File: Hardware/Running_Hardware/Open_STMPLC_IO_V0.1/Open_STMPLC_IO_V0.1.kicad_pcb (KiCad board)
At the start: 2 copper layers, 169 x 90 mm, 546 parts, among them J1 Screw_Terminal_01x10, J2 Screw_Terminal_01x06, J3 Screw_Terminal_01x04, J33 Screw_Terminal_01x02, J34 Screw_Terminal_01x02, J35 Screw_Terminal_01x03, J36 Screw_Terminal_01x03, J37 Screw_Terminal_01x03, J38 Screw_Terminal_01x03, J39 10144517-041802LF, J4 Screw_Terminal_01x02, J40 Screw_Terminal_01x04, J41 10144517-041802LF, J42 10144517-041802LF, J43 Screw_Terminal_01x02, J5 Screw_Terminal_01x04, J6 Screw_Terminal_01x04, J7 Screw_Terminal_01x04, J8 Screw_Terminal_01x04, Q1 2N7002K, Q2 2N7002K, Q3 2N7002K, Q4 2N7002K, Q5 AOD407, Q6 AOD407, Q7 MMBT5401, U1 TPS1H200A, U10 MAX31865xTP, U11 MAX31856, U12 6N137, U13 TPS1H200A, U14 TPS26600PWP, U15 NVTFS5124PLTAG, U16 TPS26600PWP, U17 NVTFS5124PLTAG, U18 TPS26600PWP, U19 NVTFS5124PLTAG, U2 TPS1H200A, U20 6N137, U21 6N137, U22 6N137, U23 6N137, U24 6N137, U25 6N137, U26 6N137, U27 6N137, U28 6N137, U29 6N137, U3 TPS1H200A, U30 6N137, U37 XTR305, U38 XTR305, U39 AD4111, U4 TPS1H200A, U40 REF3025, U41 MAX31865xTP, U5 TPS1H200A, U6 TPS1H200A, U7 TPS26600PWP, U8 NVTFS5124PLTAG, U9 TPS1H200A, Y2 16MHz

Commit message: IO board layout 1
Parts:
- added D92: SMF5V0A, Diode_SMD:D_SMF, F.Cu at (166.5, 138.5)
- added D93: SMF5V0A, Diode_SMD:D_SMF, F.Cu at (170.0, 138.5)
- added D94: SMF5V0A, Diode_SMD:D_SMF, F.Cu at (174.0, 138.5)
- added D95: SMF5V0A, Diode_SMD:D_SMF, F.Cu at (178.0, 138.5)
- added D96: SMF5V0A, Diode_SMD:D_SMF, F.Cu at (183.5, 138.5)
- added D97: SMF5V0A, Diode_SMD:D_SMF, F.Cu at (187.0, 138.5)
- added D98: SMF5V0A, Diode_SMD:D_SMF, F.Cu at (191.0, 138.5)
- added D99: SMF5V0A, Diode_SMD:D_SMF, F.Cu at (195.0, 138.5)
- C46, C47, C48, C50, C51, C69, C70, C71, C72, C73, C74, C75, C76, C77, C78, C79, C80, C90, D118, D119, D120, D121, D122, D123, D124, D125, D159, D160, D90, D91, F1, F2, F3, F4, F5, FB4, Q5, Q6, Q7, R158, R159, R160, R161, R162, R192, R193, R194, R195, R196, R197, R198, R199, R200, R201, R202, R203, R245: moved to B.Cu
- C89: value 470uF/50V -> 220uF/50V; footprint Capacitor_THT:CP_Radial_D10.0mm_P5.00mm -> Capacitor_SMD:CP_Elec_10x10.5; moved to B.Cu
- moved FB1 228.7 mm to (205.9, 127.4), turned to -90 degrees
- moved C6 228.3 mm to (204.9, 131.9), turned to 90 degrees
- moved C4 226.7 mm to (205.9, 119.4), turned to -90 degrees
- moved J4 225.7 mm to (200.0, 145.4), turned to 0 degrees
- moved R21 225.6 mm to (202.9, 134.9), turned to -90 degrees
- moved D10 225.6 mm to (201.9, 138.9), turned to 180 degrees
- moved C5 223.7 mm to (203.4, 127.4), turned to -90 degrees
- moved C7 222.0 mm to (201.9, 130.9), turned to 180 degrees
- moved R23 221.7 mm to (200.9, 134.9), turned to -90 degrees
- moved U11 219.2 mm to (201.9, 121.4), turned to 90 degrees
- moved R24 216.8 mm to (199.9, 127.4), turned to 90 degrees
- moved C11 216.5 mm to (198.9, 131.9), turned to -90 degrees
- moved D159 187.9 mm to (204.0, 87.5)
- moved D160 183.1 mm to (207.5, 70.5)
- moved R161 174.1 mm to (203.0, 85.0), turned to 180 degrees
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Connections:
- F1 pad 1: Net-(J35-Pin_3) -> Net-(J35-Pin_1)
- F2 pad 1: Net-(J36-Pin_3) -> Net-(J36-Pin_1)
- F3 pad 1: Net-(J37-Pin_3) -> Net-(J37-Pin_1)
- F4 pad 1: Net-(J38-Pin_3) -> Net-(J38-Pin_1)
- J35 pad 1: GND -> Net-(J35-Pin_1)
- J35 pad 3: Net-(J35-Pin_3) -> GND
- J36 pad 1: GND -> Net-(J36-Pin_1)
- J36 pad 3: Net-(J36-Pin_3) -> GND
- J37 pad 1: GND -> Net-(J37-Pin_1)
- J37 pad 3: Net-(J37-Pin_3) -> GND
- J38 pad 1: GND -> Net-(J38-Pin_1)
- J38 pad 3: Net-(J38-Pin_3) -> GND
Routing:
- net /DIG_IN_GRP2/COMD: track 0.00 -> 74.1 mm, vias 0 -> 1
- net /DIG_IN_GRP1/COMA: track 0.00 -> 64.3 mm, vias 0 -> 1
- net /DIG_IN_GRP2/DIG_IN_TERMINAL_12: track 0.00 -> 43.2 mm
- net /ANALOG_IN/VIN4: track 4.96 -> 46.6 mm, vias 0 -> 1
- net /DIG_IN_GRP1/DIG_IN_TERMINAL_1: track 0.00 -> 39.8 mm
- net /DIG_IN_GRP1/COMB: track 0.00 -> 39.5 mm, vias 0 -> 1
- net /DIG_IN_GRP2/COMC: track 0.00 -> 39.0 mm
- net /ANALOG_IN/VIN0: track 6.98 -> 44.4 mm, vias 0 -> 1
- net +3V3: track 145.9 -> 180.8 mm
- net /DIG_IN_GRP2/DIG_IN_TERMINAL_11: track 0.00 -> 34.4 mm
- net /DIG_IN_GRP1/DIG_IN_TERMINAL_2: track 0.00 -> 31.2 mm
- net /ANALOG_IN/IIN0+: track 0.00 -> 31.1 mm, vias 0 -> 1
- net /B2B_Connector/DIG_OUT_TERMINAL_8: track 7.88 -> 38.4 mm
- net /B2B_Connector/DIG_HS_OUT_TERMINAL_1: track 9.66 -> 39.6 mm
- net /B2B_Connector/DIG_OUT_TERMINAL_1: track 7.88 -> 37.4 mm
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
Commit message: LED arrengements
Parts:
- J39, J41, J42: moved to B.Cu
- moved D113 14.6 mm to (101.5, 125.5), turned to 90 degrees
- moved D108 14.3 mm to (80.0, 125.5), turned to 90 degrees
- moved U37 6.04 mm to (70.2, 112.1)
- moved C52 6.04 mm to (76.5, 109.5)
- moved C53 6.04 mm to (74.5, 113.0)
- moved C54 6.04 mm to (78.5, 113.0)
- moved C55 6.04 mm to (69.0, 117.0)
- moved C56 6.04 mm to (76.5, 116.0)
- moved C57 6.04 mm to (74.5, 109.5)
- moved D109 6.04 mm to (66.6, 125.5)
- moved D110 6.04 mm to (71.1, 125.5)
- moved D111 6.04 mm to (75.6, 125.5)
- moved R164 6.04 mm to (72.5, 117.0)
- moved R165 6.04 mm to (71.5, 106.5)
- moved R166 6.04 mm to (69.5, 106.5)
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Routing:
- net Net-(D112-A2): track 28.8 -> 34.8 mm
- net Net-(D114-A2): track 28.8 -> 34.8 mm
- net Net-(D114-A1): track 12.7 -> 18.7 mm
- net Net-(D110-K): track 12.7 -> 18.7 mm
- net /B2B_Connector/DIG_OUT_TERMINAL_8: track 38.4 -> 44.4 mm
- net /B2B_Connector/DIG_OUT_TERMINAL_5: track 17.2 -> 23.2 mm
- net /B2B_Connector/DIG_OUT_TERMINAL_4: track 16.7 -> 22.7 mm
- net /B2B_Connector/DIG_OUT_TERMINAL_1: track 37.4 -> 43.4 mm
- net /B2B_Connector/DIG_OUT_TERMINAL_2: track 30.0 -> 35.4 mm
- net +3V3: track 180.8 -> 175.6 mm
- net Net-(U38-SET): track 25.8 -> 29.2 mm, vias 2 -> 3
- net /ANALOG_OUT/AOUT2_V-: track 31.3 -> 34.2 mm
- net /B2B_Connector/DIG_OUT_TERMINAL_3: track 22.8 -> 25.7 mm
- net /ANALOG_IN/VIN4: track 46.6 -> 49.2 mm
- net /B2B_Connector/DIG_OUT_TERMINAL_6: track 23.6 -> 26.2 mm
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
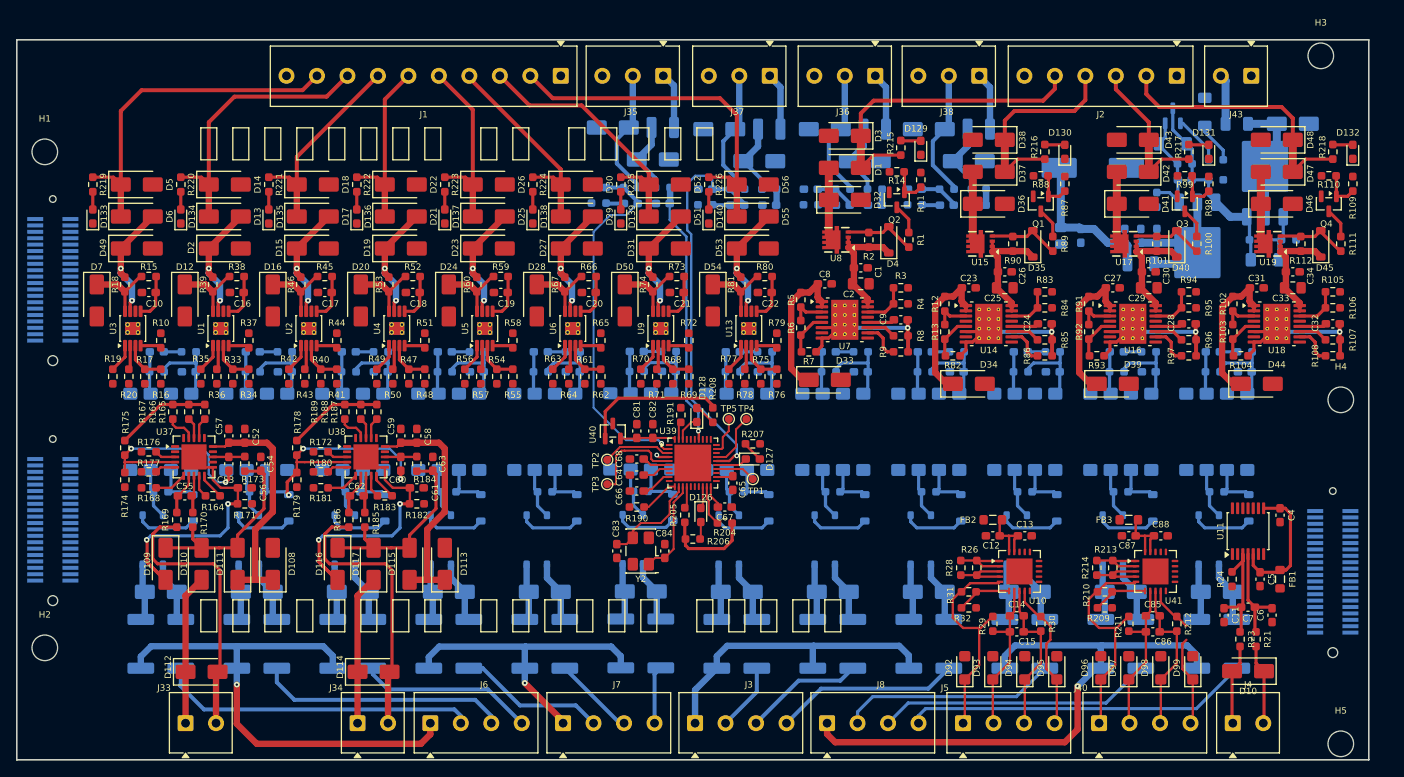
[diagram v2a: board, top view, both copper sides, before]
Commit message: Component placement IO board
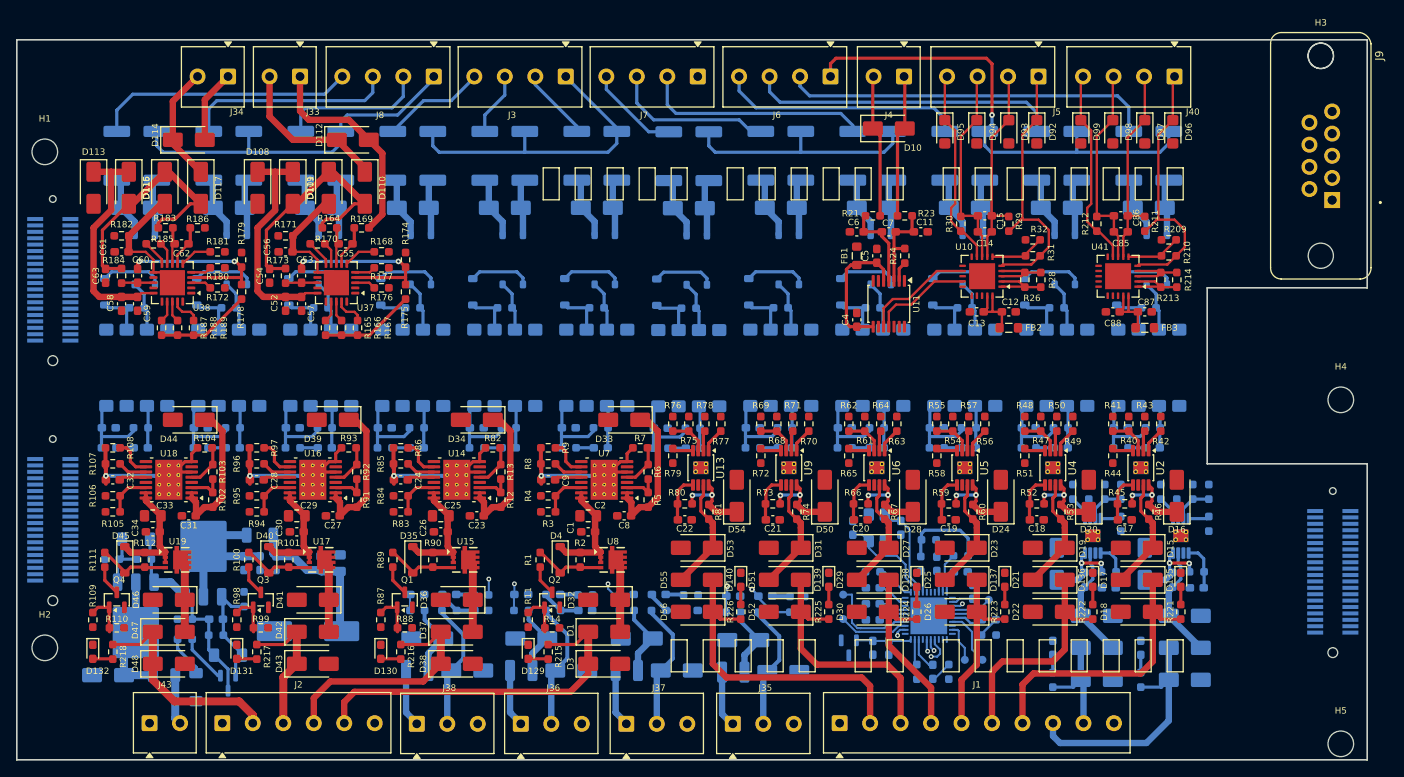
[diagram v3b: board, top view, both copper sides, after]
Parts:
- added J9: DE9_Pins, A-DF_09_PP_Z:A-DF_09_PP_Z, F.Cu at (212.4, 80.0)
- C10, C16, C64, C65, C66, C67, C68, C81, C82, C83, C84, D12, D126, D127, D128, D13, D133, D134, D14, D2, D49, D5, D6, D7, R10, R15, R16, R17, R18, R19, R190, R191, R20, R204, R205, R206, R207, R208, R219, R220, R33, R34, R35, R36, R37, R38, R39, TP1, TP2, TP3, TP4, TP5, U39, U40, Y2: moved to B.Cu
- U1, U3: footprint Package_SO:HVSSOP-8-1EP_3x3mm_P0.65mm_EP1.57x1.89mm_ThermalVias -> TPS1H200A:HVSSOP-8-1EP_3x3mm_P0.65mm_EP1.57x1.89mm_ThermalVias; moved to B.Cu
- U13, U2, U4, U5, U6, U9: footprint Package_SO:HVSSOP-8-1EP_3x3mm_P0.65mm_EP1.57x1.89mm_ThermalVias -> TPS1H200A:HVSSOP-8-1EP_3x3mm_P0.65mm_EP1.57x1.89mm_ThermalVias
- moved D132 169.4 mm to (57.5, 136.5), turned to -90 degrees
- moved R109 166.7 mm to (57.5, 132.5), turned to 90 degrees
- moved R218 164.8 mm to (60.0, 136.5), turned to 90 degrees
- moved D160 163.3 mm to (59.4, 139.4), turned to 180 degrees
- moved R110 161.7 mm to (60.5, 133.5), turned to 180 degrees
- moved J43 159.7 mm to (64.6, 145.4), turned to 0 degrees
- moved R111 159.5 mm to (59.0, 125.0), turned to 90 degrees
- moved Q4 159.4 mm to (60.5, 130.0), turned to 90 degrees
- moved R105 155.0 mm to (60.0, 119.0), turned to 180 degrees
- moved D45 154.6 mm to (61.5, 125.0), turned to -90 degrees
- moved R106 154.3 mm to (60.0, 117.0), turned to 0 degrees
- moved C32 153.7 mm to (60.0, 115.0), turned to 180 degrees
- moved R107 153.3 mm to (60.0, 113.0), turned to 0 degrees
- moved D48 153.2 mm to (67.0, 138.0), turned to 0 degrees
- moved R108 152.9 mm to (60.0, 111.0), turned to 0 degrees
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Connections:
- J33 pad 1: Net-(D110-K) -> Net-(D112-A2)
- J33 pad 2: Net-(D112-A2) -> Net-(D110-K)
- J34 pad 1: Net-(D114-A1) -> Net-(D114-A2)
- J34 pad 2: Net-(D114-A2) -> Net-(D114-A1)
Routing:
- net /ANALOG_IN/COMPA: track 0.00 -> 64.9 mm, vias 0 -> 2
- net /ANALOG_IN/IIN1+: track 2.02 -> 64.6 mm, vias 0 -> 2
- net /ANALOG_IN/IIN2+: track 2.02 -> 52.7 mm, vias 0 -> 2
- net /ANALOG_IN/VIN4: track 49.2 -> 7.78 mm, vias 1 -> 0
- net /B2B_Connector/DIG_OUT_TERMINAL_1: track 43.4 -> 13.4 mm
- net /DIG_IN_GRP2/COMD: track 74.1 -> 45.1 mm, vias 1 -> 0
- net Net-(D114-A2): track 34.8 -> 9.12 mm
- net +3V3: track 175.6 -> 157.4 mm
- net /ANALOG_OUT/AOUT2_V-: track 34.2 -> 16.2 mm, vias 2 -> 0
- net /ANALOG_OUT/AOUT1_V-: track 34.2 -> 16.2 mm, vias 2 -> 0
- net /ANALOG_IN/VIN0: track 45.8 -> 30.1 mm, vias 1 -> 2
- net /B2B_Connector/TEMP_SCLK: track 0.00 -> 14.1 mm
- net /B2B_Connector/TEMP_MISO: track 0.00 -> 12.7 mm
- net /B2B_Connector/DIG_OUT_TERMINAL_3: track 25.7 -> 36.4 mm
- net /DIG_IN_GRP2/DIG_IN_TERMINAL_12: track 43.2 -> 32.6 mm
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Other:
- board size 169 x 90 mm -> 168.8 x 90 mm
- copper layers 2 -> 4

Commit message: IO board layout
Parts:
- D126, D127, D128, D133, D134, D141, D142, D143, D144, D145, D146, D147, D148, D149, D150, D151, D152, R206, R207, R208, R219, R220, R227, R228, R229, R230, R231, R232, R233, R234, R235, R236, R237, R238: moved to F.Cu
- moved D132 73.3 mm to (130.8, 137.0), turned to 90 degrees
- moved R218 68.8 mm to (128.8, 137.0), turned to -90 degrees
- moved R238 62.7 mm to (112.8, 78.0), turned to 90 degrees
- moved D152 61.0 mm to (114.8, 78.0), turned to -90 degrees
- moved D131 59.3 mm to (134.8, 137.0), turned to 90 degrees
- moved R237 56.4 mm to (116.8, 78.0), turned to 90 degrees
- moved D151 54.8 mm to (118.8, 78.0), turned to -90 degrees
- moved R217 54.8 mm to (132.8, 137.0), turned to -90 degrees
- moved R236 50.6 mm to (120.8, 78.0), turned to 90 degrees
- moved D150 49.1 mm to (122.8, 78.0), turned to -90 degrees
- moved D130 45.3 mm to (138.8, 137.0), turned to 90 degrees
- moved R235 45.1 mm to (124.8, 78.0), turned to 90 degrees
- moved D149 43.8 mm to (126.8, 78.0), turned to -90 degrees
- moved D141 41.5 mm to (164.8, 78.0), turned to -90 degrees
- moved R216 40.8 mm to (136.8, 137.0), turned to -90 degrees
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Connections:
- net Net-(D126-K) renamed /ANALOG_IN/ANALOG_IN_ERROR
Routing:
- net +3V3: track 157.4 -> 294.7 mm, vias 0 -> 4
- net /ANALOG_IN/IIN3+: track 2.02 -> 100.2 mm, vias 0 -> 2
- net /ANALOG_IN/VIN6: track 4.96 -> 87.8 mm, vias 0 -> 2
- net /B2B_Connector/DIG_IN_12: track 5.31 -> 82.8 mm, vias 0 -> 2
- net /B2B_Connector/DIG_IN_11: track 5.31 -> 75.5 mm, vias 0 -> 2
- net /B2B_Connector/DIG_IN_10: track 5.31 -> 67.9 mm, vias 0 -> 2
- net /B2B_Connector/DIG_IN_1: track 5.31 -> 61.6 mm, vias 0 -> 2
- net /B2B_Connector/DIG_IN_9: track 5.31 -> 60.6 mm, vias 0 -> 2
- net /B2B_Connector/DIG_HS_OUT_TERMINAL_1: track 45.5 -> 97.4 mm, vias 0 -> 1
- net /B2B_Connector/DIG_HS_OUT_TERMINAL_3: track 17.8 -> 69.7 mm, vias 0 -> 1
- net /B2B_Connector/DIG_HS_OUT_TERMINAL_2: track 30.4 -> 81.6 mm, vias 0 -> 1
- net /ANALOG_IN/VIN4: track 7.78 -> 58.9 mm, vias 0 -> 2
- net /B2B_Connector/DIG_HS_OUT_TERMINAL_4: track 27.0 -> 77.9 mm, vias 0 -> 1
- net /B2B_Connector/DIG_IN_2: track 5.31 -> 53.9 mm, vias 0 -> 2
- net /B2B_Connector/DIG_IN_8: track 5.31 -> 53.4 mm, vias 0 -> 2
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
